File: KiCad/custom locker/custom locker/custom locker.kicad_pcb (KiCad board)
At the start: 2 copper layers, 8 parts, among them J1 servo motor connector, J3 HX711 load cell, SW1 SW_Push, SW2 SW_Push, SW3 SW_Push, U1 ESP32-DEVKITC-32D, U2 DM-OLED096-636

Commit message: finished pcb
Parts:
- added DOWN1: SW_Push, Button_Switch_Keyboard:SW_Cherry_MX_1.00u_PCB, F.Cu at (88.1, 57.1)
- added J2: Power, Connector_PinHeader_2.54mm:PinHeader_1x02_P2.54mm_Vertical, B.Cu at (16.0, 32.0)
- added J4: Hall Effect Sensor, Connector_PinHeader_2.54mm:PinHeader_1x03_P2.54mm_Vertical, B.Cu at (16.0, 42.0)
- J1: value servo motor connector -> Servo Motor Connector
- moved CANCEL1 26.9 mm to (97.0, 38.0)
- moved UP1 9.95 mm to (87.9, 19.0)
- moved J1 5.39 mm to (16.0, 37.0)
- moved U1 1.66 mm to (39.3, 59.0)
- moved J3 1.07 mm to (33.0, 31.6)
- renumbered SW3 to CANCEL1, SW2 to SELECT1, SW1 to UP1
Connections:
- U1 pad J2-5: unconnected-(U1-IO34-PadJ2-5) -> Net-(J4-Pin_3)
- U1 pad J3-12: unconnected-(U1-IO16-PadJ3-12) -> SW4
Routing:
- net GND: track 0.00 -> 190.6 mm, vias 0 -> 7
- net +5V: track 0.00 -> 83.2 mm, vias 0 -> 1
- net SW1: track 0.00 -> 68.8 mm, vias 0 -> 1
- net Net-(U1-IO32): track 0.00 -> 56.4 mm, vias 0 -> 2
- net SW4: track 0.00 -> 56.2 mm, vias 0 -> 1
- net SW3: track 0.00 -> 54.8 mm, vias 0 -> 1
- net Clock: track 0.00 -> 47.9 mm, vias 0 -> 4
- net Net-(J4-Pin_3): track 0.00 -> 46.6 mm, vias 0 -> 4
- net SW2: track 0.00 -> 41.7 mm, vias 0 -> 1
- net Net-(J1-Pin_3): track 0.00 -> 40.6 mm
- net /I²C Data: track 0.00 -> 33.6 mm, vias 0 -> 1
- net /I²C Clock: track 0.00 -> 33.4 mm, vias 0 -> 1
- net /Data: track 0.00 -> 27.9 mm, vias 0 -> 2
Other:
- board outline added: 92 x 62 mm

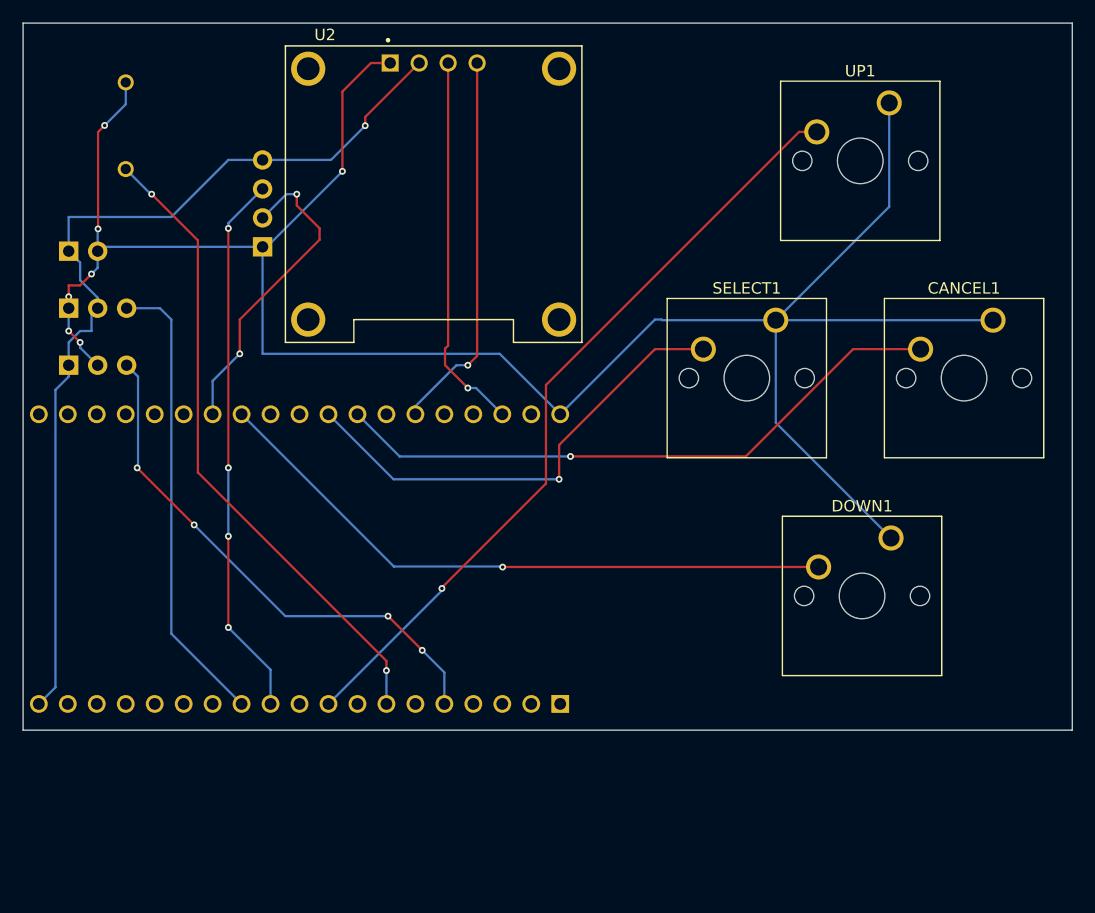
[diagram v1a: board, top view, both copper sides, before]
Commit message: little changes on PCB
mainly added screw holes
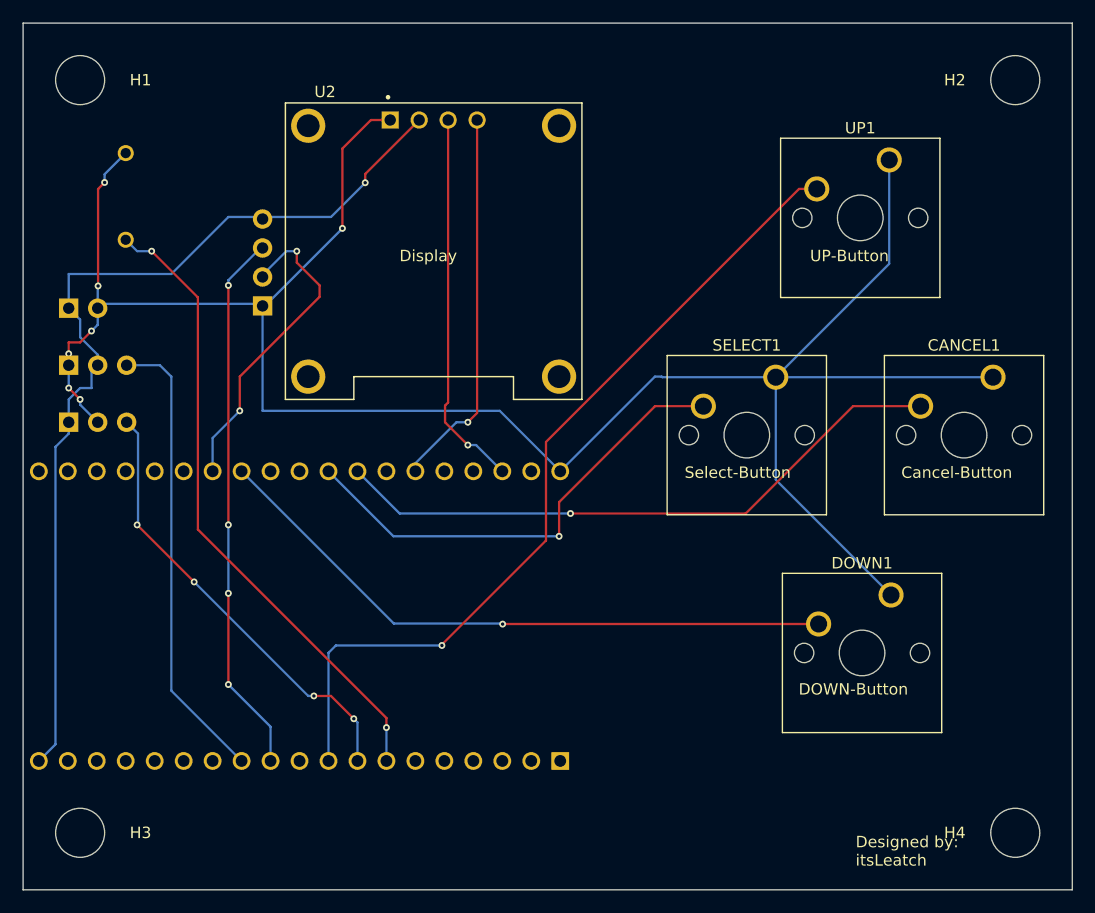
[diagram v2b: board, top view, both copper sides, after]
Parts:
- added H1: MountingHole, MountingHole:MountingHole_4.3mm_M4, F.Cu at (17.0, 17.0)
- added H2: MountingHole, MountingHole:MountingHole_4.3mm_M4, F.Cu at (99.0, 17.0)
- added H3: MountingHole, MountingHole:MountingHole_4.3mm_M4, F.Cu at (17.0, 83.0)
- added H4: MountingHole, MountingHole:MountingHole_4.3mm_M4, F.Cu at (99.0, 83.0)
- moved LS1 6.20 mm to (21.0, 27.2)
- moved J3 5.18 mm to (33.0, 36.8)
- moved CANCEL1 5.00 mm to (97.0, 43.0)
- moved DOWN1 5.00 mm to (88.1, 62.1)
- moved J1 5.00 mm to (16.0, 42.0)
- moved J2 5.00 mm to (16.0, 37.0)
- moved J4 5.00 mm to (16.0, 47.0)
- moved SELECT1 5.00 mm to (78.0, 43.0)
- moved U1 5.00 mm to (39.3, 64.0)
- moved U2 5.00 mm to (48.0, 32.0)
- moved UP1 5.00 mm to (87.9, 24.0)
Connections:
- U1 pad J2-5: Net-(J4-Pin_3) -> unconnected-(U1-IO34-PadJ2-5)
- U1 pad J2-8: unconnected-(U1-IO33-PadJ2-8) -> Net-(J4-Pin_3)
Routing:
- net Net-(J4-Pin_3): track 46.6 -> 39.3 mm
- net SW1: track 68.8 -> 74.4 mm
- net GND: track 190.6 -> 189.4 mm
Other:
- board size 92 x 62 mm -> 92 x 76 mm
- board text added: "Buzzer"
- board text added: "Cancel-Button"
- board text added: "DOWN-Button"
- board text added: "Designed by: itsLeatch"
- board text added: "Display"
- board text added: "ESP-32 Here"
- board text added: "HX711 load cell"
- board text added: "Hall Effect Sensor"
- board text added: "Power"
- board text added: "Select-Button"
- board text added: "Servo Motor Connector"
- board text added: "UP-Button"

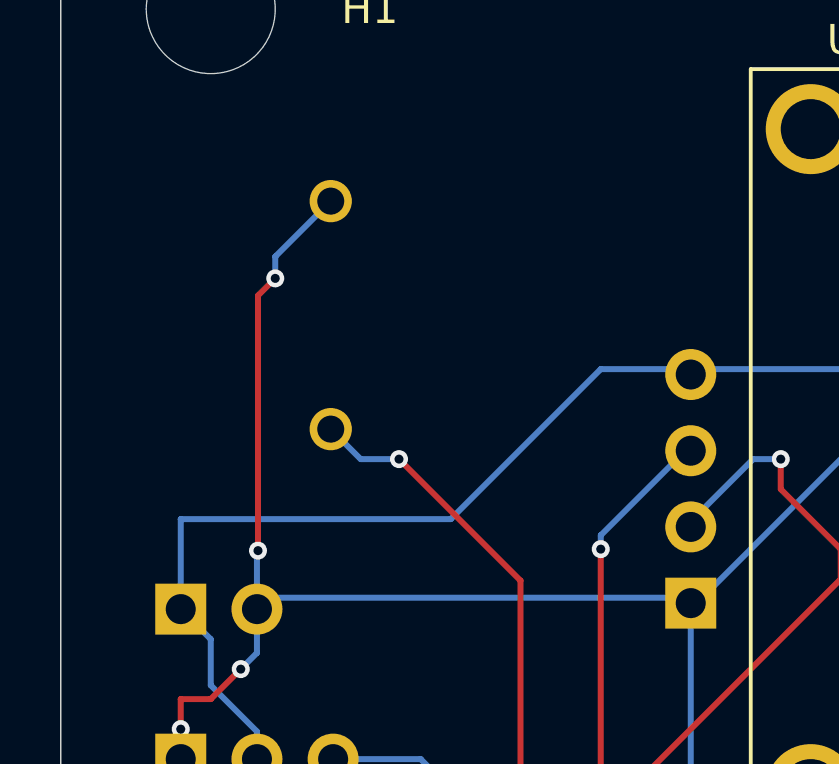
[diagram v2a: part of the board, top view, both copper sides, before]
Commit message: small PCB changes
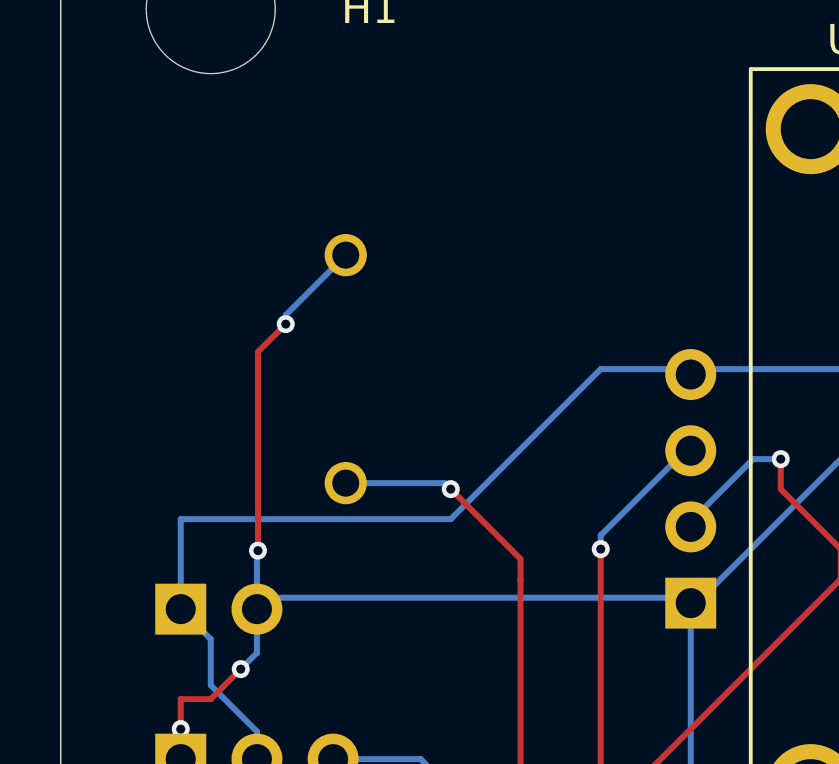
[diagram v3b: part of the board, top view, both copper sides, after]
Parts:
- moved LS1 1.87 mm to (21.5, 29.0)
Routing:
- net GND: track 189.4 -> 187.8 mm
- net Net-(U1-IO32): track 55.9 -> 55.1 mm
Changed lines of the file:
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@@
 	(footprint "KXG1203C:XDCR_KXG1203C"
 		(layer "B.Cu")
-		(at 21 27.2 90)
+		(at 21.5 29 90)
 		(property "Reference" "LS1"
 			(at -2.595 7.465 90)
@@
 	)
 	(gr_text "Power\n"
-		(at 25 38 0)
+		(at 25 38.5 0)
 		(layer "B.SilkS")
 		(effects
@@
 	)
 	(segment
-		(start 18.575 35.05)
-		(end 18.575 26.55)
-		(width 0.2)
-		(layer "F.Cu")
-		(net 1)
-	)
-	(segment
 		(start 42.5 20.5)
 		(end 44.19 20.5)
@@
 	)
 	(segment
+		(start 18.575 28.425)
+		(end 19.5 27.5)
+		(width 0.2)
+		(layer "F.Cu")
+		(net 1)
+	)
+	(segment
+		(start 18.575 35.05)
+		(end 18.575 28.425)
+		(width 0.2)
+		(layer "F.Cu")
+		(net 1)
+	)
+	(segment
 		(start 17 40)
 		(end 16 40)
@@
 		(start 18 39)
 		(end 17 40)
-		(width 0.2)
-		(layer "F.Cu")
-		(net 1)
-	)
-	(segment
-		(start 18.575 26.55)
-		(end 19.15 25.975)
 		(width 0.2)
 		(layer "F.Cu")
@@
 	)
 	(via
-		(at 19.15 25.975)
-		(size 0.6)
-		(drill 0.3)
-		(layers "F.Cu" "B.Cu")
-		(net 1)
-	)
-	(via
 		(at 17 45)
 		(size 0.6)
@@
 		(net 1)
 	)
+	(via
+		(at 19.5 27.5)
+		(size 0.6)
+		(drill 0.3)
+		(layers "F.Cu" "B.Cu")
+		(net 1)
+	)
 	(segment
 		(start 59.1 51.3)
@@
 	)
 	(segment
-		(start 19.15 25.25)
-		(end 21 23.4)
-		(width 0.2)
-		(layer "B.Cu")
-		(net 1)
-	)
-	(segment
 		(start 59.1 51.3)
 		(end 53.8 46)
@@
 	)
 	(segment
+		(start 19.5 27.5)
+		(end 19.5 27.2)
+		(width 0.2)
+		(layer "B.Cu")
+		(net 1)
+	)
+	(segment
 		(start 33 36.62)
 		(end 18.92 36.62)
@@
 	)
 	(segment
-		(start 19.15 25.975)
-		(end 19.15 25.25)
-		(width 0.2)
-		(layer "B.Cu")
-		(net 1)
-	)
-	(segment
 		(start 78 43.05)
 		(end 87.9475 33.1025)
@@
 		(start 16 42)
 		(end 16 44)
+		(width 0.2)
+		(layer "B.Cu")
+		(net 1)
+	)
+	(segment
+		(start 19.5 27.2)
+		(end 21.5 25.2)
 		(width 0.2)
 		(layer "B.Cu")
@@
 	(segment
 		(start 27.325 36.05)
-		(end 23.275 32)
+		(end 27.325 35.325)
 		(width 0.2)
 		(layer "F.Cu")
@@
 		(net 15)
 	)
+	(segment
+		(start 27.325 35.325)
+		(end 25 33)
+		(width 0.2)
+		(layer "F.Cu")
+		(net 15)
+	)
 	(via
-		(at 23.275 32)
+		(at 25 33)
 		(size 0.6)
 		(drill 0.3)
@@
 	)
 	(segment
-		(start 23.275 32)
-		(end 22 32)
+		(start 25 33)
+		(end 24.8 32.8)
 		(width 0.2)
 		(layer "B.Cu")
@@
 	)
 	(segment
-		(start 22 32)
-		(end 21 31)
-		(width 0.2)
-		(layer "B.Cu")
+		(start 24.8 32.8)
+		(end 21.5 32.8)
+		(width 0.2)
+		(layer "B.Cu")
